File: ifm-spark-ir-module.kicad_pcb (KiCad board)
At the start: 2 copper layers, 4 parts, among them J1 CONN_01X03_MALE

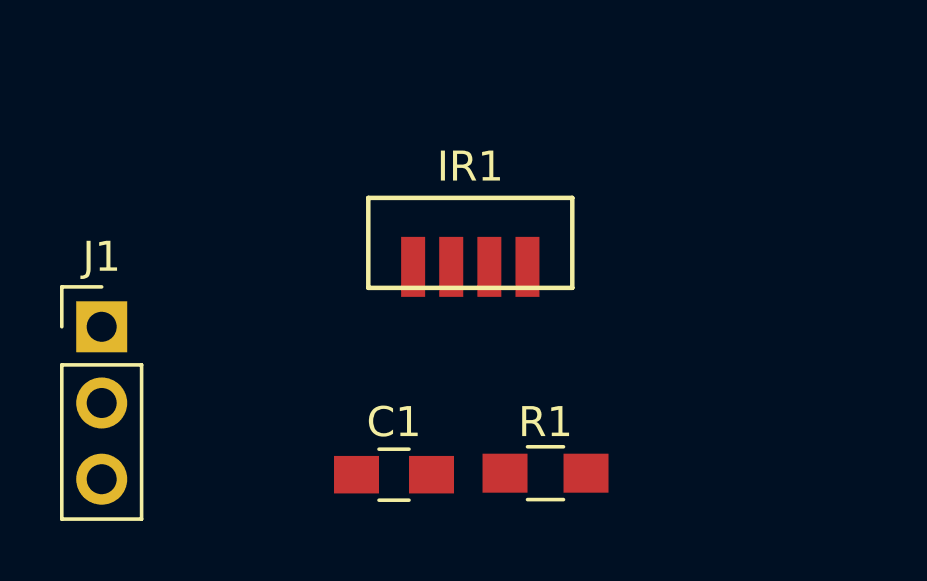
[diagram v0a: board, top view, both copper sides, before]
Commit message: Filled ground-plane
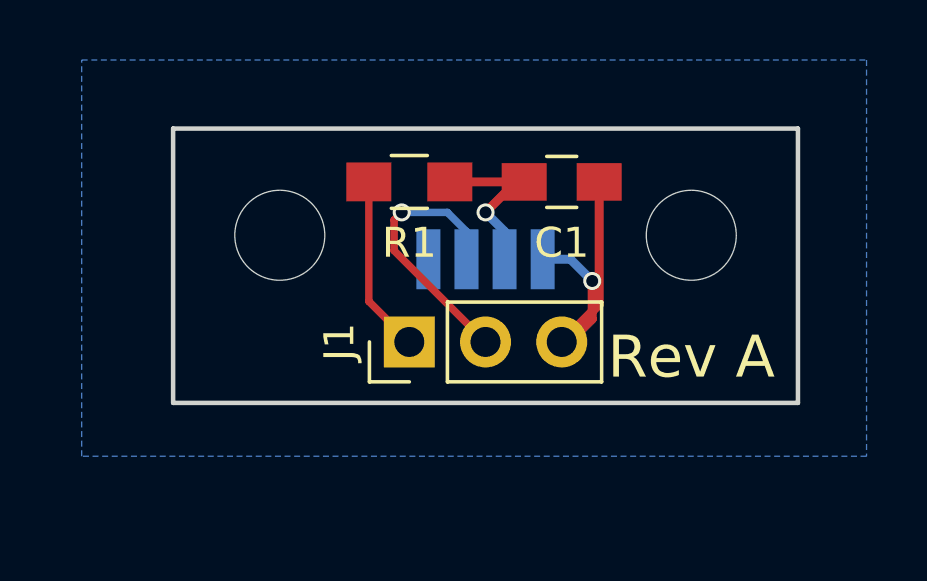
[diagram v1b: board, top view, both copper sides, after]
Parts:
- added REF**: MountingHole_3mm, Mounting_Holes:MountingHole_3mm, F.Cu at (55.4, 34.0)
- added REF**: MountingHole_3mm, Mounting_Holes:MountingHole_3mm, F.Cu at (41.7, 34.0)
- IR1: moved to B.Cu
- moved C1 11.2 mm to (51.1, 32.3)
- moved R1 10.7 mm to (46.0, 32.3)
- moved J1 10.3 mm to (46.0, 37.6), turned to 90 degrees
- moved IR1 0.57 mm to (48.5, 34.0), turned to 180 degrees
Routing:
- net GND: track 0.00 -> 10.4 mm, vias 0 -> 1
- net Net-(IR1-Pad3): track 0.00 -> 9.03 mm, vias 0 -> 1
- net Net-(C1-Pad1): track 0.00 -> 6.02 mm, vias 0 -> 1
- net Net-(J1-Pad1): track 0.00 -> 5.89 mm
- added copper zone on B.Cu, net GND
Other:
- board outline added: 20.8 x 9.1 mm
- rule pad_to_mask_clearance: 0.2 -> 0.05
- board text added: "Rev A"
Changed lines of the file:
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@@
   (general
     (links 7)
-    (no_connects 7)
-    (area 165.608 94.742 190.59562 106.532)
+    (no_connects 0)
+    (area 38.024999 30.404999 59.003001 39.699001)
     (thickness 1.6)
-    (drawings 0)
-    (tracks 0)
+    (drawings 5)
+    (tracks 23)
     (zones 0)
-    (modules 4)
+    (modules 6)
     (nets 5)
   )
@@
     (pad_size 1.524 1.524)
     (pad_drill 0.762)
-    (pad_to_mask_clearance 0.2)
+    (pad_to_mask_clearance 0.05)
     (aux_axis_origin 0 0)
-    (visible_elements FFFFFF7F)
+    (visible_elements FFFFFFFF)
     (pcbplotparams
       (layerselection 0x00030_80000001)
@@
   )
   (module Capacitors_SMD:C_0805_HandSoldering (layer F.Cu)
-    (at 45.463001 42.017)
+    (at 51.054 32.258)
     (descr "Capacitor SMD 0805, hand soldering")
     (tags "capacitor 0805")
     (attr smd)
-    (fp_text reference C1 (at 0 -1.75) (layer F.SilkS)
+    (fp_text reference C1 (at 0 2.032) (layer F.SilkS)
       (effects (font (size 1 1) (thickness 0.15)))
     )
@@
       (effects (font (size 1 1) (thickness 0.15)))
     )
-    (fp_text user %R (at 0 -1.75) (layer F.Fab)
+    (fp_text user %R (at 0 2.032) (layer F.Fab)
       (effects (font (size 1 1) (thickness 0.15)))
     )
@@
     )
   )
-  (module ifm-ic-digital:TSOP75x (layer F.Cu)
-    (at 48.006 34.29)
-    (fp_text reference IR1 (at 0 -2.54) (layer F.SilkS)
-      (effects (font (size 1 1) (thickness 0.15)))
-    )
-    (fp_text value TSOP75338TT (at 0 -1.27) (layer F.Fab)
-      (effects (font (size 1 1) (thickness 0.15)))
-    )
-    (fp_line (start -3.4 -1.5) (end -3.4 1.5) (layer F.SilkS) (width 0.15))
-    (fp_line (start -3.4 1.5) (end 3.4 1.5) (layer F.SilkS) (width 0.15))
-    (fp_line (start 3.4 -1.5) (end 3.4 1.5) (layer F.SilkS) (width 0.15))
-    (fp_line (start -3.4 -1.5) (end 3.4 -1.5) (layer F.SilkS) (width 0.15))
-    (pad 1 smd rect (at -1.905 0.8) (size 0.8 2) (layers F.Cu F.Paste F.Mask)
+  (module ifm-ic-digital:TSOP75x (layer B.Cu)
+    (at 48.514 34.036 180)
+    (fp_text reference IR1 (at 0 2.54 180) (layer B.SilkS)
+      (effects (font (size 1 1) (thickness 0.15)) (justify mirror))
+    )
+    (fp_text value TSOP75338TT (at 0 1.27 180) (layer B.Fab)
+      (effects (font (size 1 1) (thickness 0.15)) (justify mirror))
+    )
+    (fp_line (start -3.4 1.5) (end -3.4 -1.5) (layer B.SilkS) (width 0.15))
+    (fp_line (start -3.4 -1.5) (end 3.4 -1.5) (layer B.SilkS) (width 0.15))
+    (fp_line (start 3.4 1.5) (end 3.4 -1.5) (layer B.SilkS) (width 0.15))
+    (fp_line (start -3.4 1.5) (end 3.4 1.5) (layer B.SilkS) (width 0.15))
+    (pad 1 smd rect (at -1.905 -0.8 180) (size 0.8 2) (layers B.Cu B.Paste B.Mask)
       (net 2 GND))
-    (pad 2 smd rect (at -0.635 0.8) (size 0.8 2) (layers F.Cu F.Paste F.Mask)
+    (pad 2 smd rect (at -0.635 -0.8 180) (size 0.8 2) (layers B.Cu B.Paste B.Mask)
       (net 1 "Net-(C1-Pad1)"))
-    (pad 3 smd rect (at 0.635 0.8) (size 0.8 2) (layers F.Cu F.Paste F.Mask)
+    (pad 3 smd rect (at 0.635 -0.8 180) (size 0.8 2) (layers B.Cu B.Paste B.Mask)
       (net 3 "Net-(IR1-Pad3)"))
-    (pad 4 smd rect (at 1.905 0.8) (size 0.8 2) (layers F.Cu F.Paste F.Mask)
+    (pad 4 smd rect (at 1.905 -0.8 180) (size 0.8 2) (layers B.Cu B.Paste B.Mask)
       (net 2 GND))
   )
   (module Pin_Headers:Pin_Header_Straight_1x03_Pitch2.54mm (layer F.Cu)
-    (at 35.719429 37.087)
+    (at 45.974 37.592 90)
     (descr "Through hole straight pin header, 1x03, 2.54mm pitch, single row")
     (tags "Through hole pin header THT 1x03 2.54mm single row")
-    (fp_text reference J1 (at 0 -2.33) (layer F.SilkS)
-      (effects (font (size 1 1) (thickness 0.15)))
-    )
-    (fp_text value CONN_01X03_MALE (at 0 7.41) (layer F.Fab)
+    (fp_text reference J1 (at 0 -2.33 90) (layer F.SilkS)
+      (effects (font (size 1 1) (thickness 0.15)))
+    )
+    (fp_text value CONN_01X03_MALE (at 0 7.41 90) (layer F.Fab)
       (effects (font (size 1 1) (thickness 0.15)))
     )
@@
     (fp_line (start 1.8 6.85) (end 1.8 -1.8) (layer F.CrtYd) (width 0.05))
     (fp_line (start 1.8 -1.8) (end -1.8 -1.8) (layer F.CrtYd) (width 0.05))
-    (fp_text user %R (at 0 -2.33) (layer F.Fab)
-      (effects (font (size 1 1) (thickness 0.15)))
-    )
-    (pad 1 thru_hole rect (at 0 0) (size 1.7 1.7) (drill 1) (layers *.Cu *.Mask)
+    (fp_text user %R (at 0 -2.33 90) (layer F.Fab)
+      (effects (font (size 1 1) (thickness 0.15)))
+    )
+    (pad 1 thru_hole rect (at 0 0 90) (size 1.7 1.7) (drill 1) (layers *.Cu *.Mask)
       (net 4 "Net-(J1-Pad1)"))
-    (pad 2 thru_hole oval (at 0 2.54) (size 1.7 1.7) (drill 1) (layers *.Cu *.Mask)
+    (pad 2 thru_hole oval (at 0 2.54 90) (size 1.7 1.7) (drill 1) (layers *.Cu *.Mask)
       (net 3 "Net-(IR1-Pad3)"))
-    (pad 3 thru_hole oval (at 0 5.08) (size 1.7 1.7) (drill 1) (layers *.Cu *.Mask)
+    (pad 3 thru_hole oval (at 0 5.08 90) (size 1.7 1.7) (drill 1) (layers *.Cu *.Mask)
       (net 2 GND))
     (model ${KISYS3DMOD}/Pin_Headers.3dshapes/Pin_Header_Straight_1x03_Pitch2.54mm.wrl
@@
   )
   (module Resistors_SMD:R_0805_HandSoldering (layer F.Cu)
-    (at 50.513001 41.967)
+    (at 45.974 32.258)
     (descr "Resistor SMD 0805, hand soldering")
     (tags "resistor 0805")
     (attr smd)
-    (fp_text reference R1 (at 0 -1.7) (layer F.SilkS)
+    (fp_text reference R1 (at 0 2.032) (layer F.SilkS)
       (effects (font (size 1 1) (thickness 0.15)))
     )
@@
     )
   )
+  (module Mounting_Holes:MountingHole_3mm (layer F.Cu)
+    (at 55.372 34.036)
+    (descr "Mounting Hole 3mm, no annular")
+    (tags "mounting hole 3mm no annular")
+    (fp_text reference REF** (at 0 -4) (layer F.SilkS) hide
+      (effects (font (size 1 1) (thickness 0.15)))
+    )
+    (fp_text value MountingHole_3mm (at 0 4) (layer F.Fab)
+      (effects (font (size 1 1) (thickness 0.15)))
+    )
+    (fp_circle (center 0 0) (end 3 0) (layer Cmts.User) (width 0.15))
+    (fp_circle (center 0 0) (end 3.25 0) (layer F.CrtYd) (width 0.05))
+    (pad 1 np_thru_hole circle (at 0 0) (size 3 3) (drill 3) (layers *.Cu *.Mask))
+  )
+  (module Mounting_Holes:MountingHole_3mm (layer F.Cu)
+    (at 41.656 34.036)
+    (descr "Mounting Hole 3mm, no annular")
+    (tags "mounting hole 3mm no annular")
+    (fp_text reference REF** (at 0 -4) (layer F.SilkS) hide
+      (effects (font (size 1 1) (thickness 0.15)))
+    )
+    (fp_text value MountingHole_3mm (at 0 4) (layer F.Fab)
+      (effects (font (size 1 1) (thickness 0.15)))
+    )
+    (fp_circle (center 0 0) (end 3 0) (layer Cmts.User) (width 0.15))
+    (fp_circle (center 0 0) (end 3.25 0) (layer F.CrtYd) (width 0.05))
+    (pad 1 np_thru_hole circle (at 0 0) (size 3 3) (drill 3) (layers *.Cu *.Mask))
+  )
+  (gr_text "Rev A" (at 55.372 38.1) (layer F.SilkS)
+    (effects (font (size 1.4 1.4) (thickness 0.3)))
+  )
+  (gr_line (start 38.1 39.624) (end 38.1 30.48) (angle 90) (layer Edge.Cuts) (width 0.15))
+  (gr_line (start 58.928 39.624) (end 38.1 39.624) (angle 90) (layer Edge.Cuts) (width 0.15))
+  (gr_line (start 58.928 30.48) (end 58.928 39.624) (angle 90) (layer Edge.Cuts) (width 0.15))
+  (gr_line (start 38.1 30.48) (end 58.928 30.48) (angle 90) (layer Edge.Cuts) (width 0.15))
+  (segment (start 49.804 32.258) (end 49.53 32.258) (width 0.3) (layer F.Cu) (net 1))
+  (segment (start 49.53 32.258) (end 48.514 33.274) (width 0.3) (layer F.Cu) (net 1))
+  (segment (start 48.514 33.274) (end 49.149 33.909) (width 0.3) (layer B.Cu) (net 1))
+  (via (at 48.514 33.274) (size 0.6) (drill 0.4) (layers F.Cu B.Cu) (net 1))
+  (segment (start 49.149 33.909) (end 49.149 34.836) (width 0.3) (layer B.Cu) (net 1))
+  (segment (start 47.324 32.258) (end 49.804 32.258) (width 0.3) (layer F.Cu) (net 1))
+  (segment (start 52.304 32.258) (end 52.304 36.342) (width 0.3) (layer F.Cu) (net 2))
+  (segment (start 52.304 36.342) (end 51.054 37.592) (width 0.3) (layer F.Cu) (net 2))
+  (segment (start 50.419 34.836) (end 51.346 34.836) (width 0.3) (layer B.Cu) (net 2))
+  (segment (start 52.07 36.83) (end 51.308 37.592) (width 0.3) (layer F.Cu) (net 2))
+  (segment (start 52.07 35.56) (end 52.07 36.83) (width 0.3) (layer F.Cu) (net 2))
+  (via (at 52.07 35.56) (size 0.6) (drill 0.4) (layers F.Cu B.Cu) (net 2))
+  (segment (start 51.346 34.836) (end 52.07 35.56) (width 0.3) (layer B.Cu) (net 2))
+  (segment (start 51.308 37.592) (end 51.054 37.592) (width 0.3) (layer F.Cu) (net 2))
+  (segment (start 47.879 34.836) (end 47.879 33.909) (width 0.25) (layer B.Cu) (net 3))
+  (segment (start 47.879 33.909) (end 47.244 33.274) (width 0.25) (layer B.Cu) (net 3))
+  (segment (start 47.244 33.274) (end 45.72 33.274) (width 0.25) (layer B.Cu) (net 3))
+  (via (at 45.72 33.274) (size 0.6) (drill 0.4) (layers F.Cu B.Cu) (net 3))
+  (segment (start 45.72 33.274) (end 45.466 33.528) (width 0.25) (layer F.Cu) (net 3))
+  (segment (start 45.466 33.528) (end 45.466 34.544) (width 0.25) (layer F.Cu) (net 3))
+  (segment (start 45.466 34.544) (end 48.514 37.592) (width 0.25) (layer F.Cu) (net 3))
+  (segment (start 44.624 32.258) (end 44.624 36.242) (width 0.25) (layer F.Cu) (net 4))
+  (segment (start 44.624 36.242) (end 45.974 37.592) (width 0.25) (layer F.Cu) (net 4))
+  (zone (net 2) (net_name GND) (layer B.Cu) (hatch edge 0.508)
+    (connect_pads (clearance 0.508))
+    (min_thickness 0.254)
+    (fill yes (arc_segments 16) (thermal_gap 0.508) (thermal_bridge_width 0.508))
+    (polygon
+      (pts
+        (xy 61.214 41.402) (xy 35.052 41.402) (xy 35.052 28.194) (xy 61.214 28.194)
+      )
+    )
+  )
